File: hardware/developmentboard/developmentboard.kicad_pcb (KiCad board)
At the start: 2 copper layers, 207.5 x 78.1 mm, 35 parts, among them J1 SPI Header, J2 Power Header, J3 Key Channels, U1 ADS7960, U10 DRV5053, U11 DRV5053, U12 DRV5053, U13 DRV5053, U14 AP2138N-2.5, U2 DRV5053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

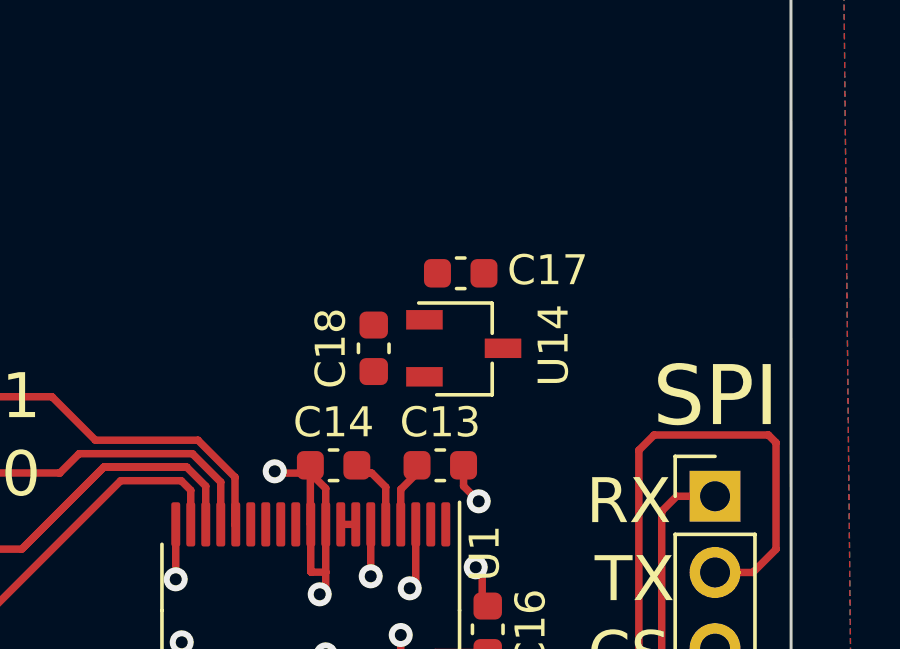
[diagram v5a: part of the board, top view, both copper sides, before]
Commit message: added reference IC to PCB, removed LDO
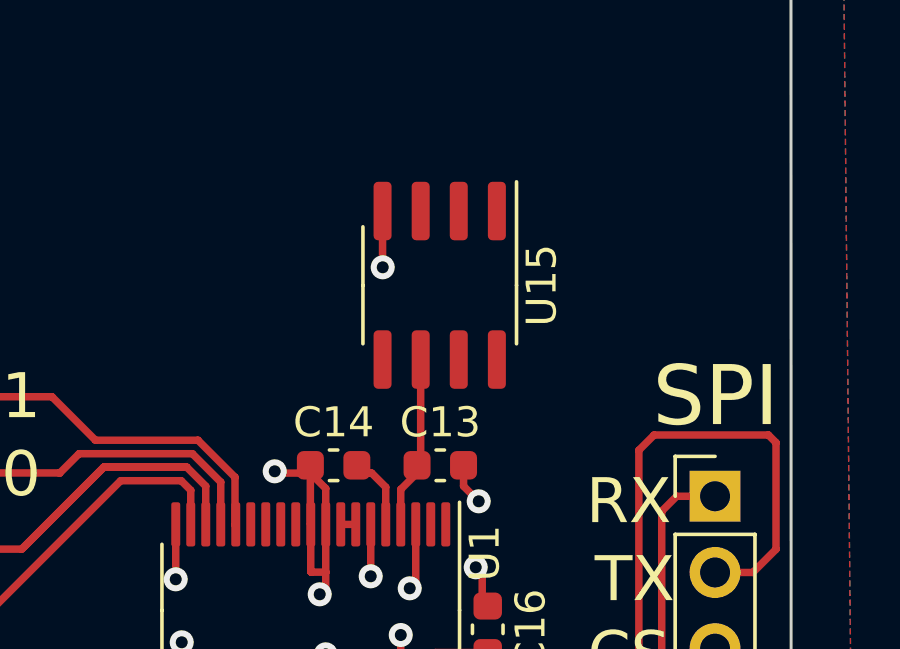
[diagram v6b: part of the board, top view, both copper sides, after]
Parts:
- removed C17, C18: 1uF, Capacitor_SMD:C_0603_1608Metric
- removed U14: AP2138N-2.5, Package_TO_SOT_SMD:TSOT-23
- added U15: REF5025AD, Package_SO:SOIC-8_3.9x4.9mm_P1.27mm, F.Cu at (249.4, 83.7)
- J3: value Key Channels -> Hall Effect Header
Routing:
- net +2V5: track 1.93 -> 5.51 mm
- net GND: track 54.4 -> 56.3 mm, vias 35 -> 36

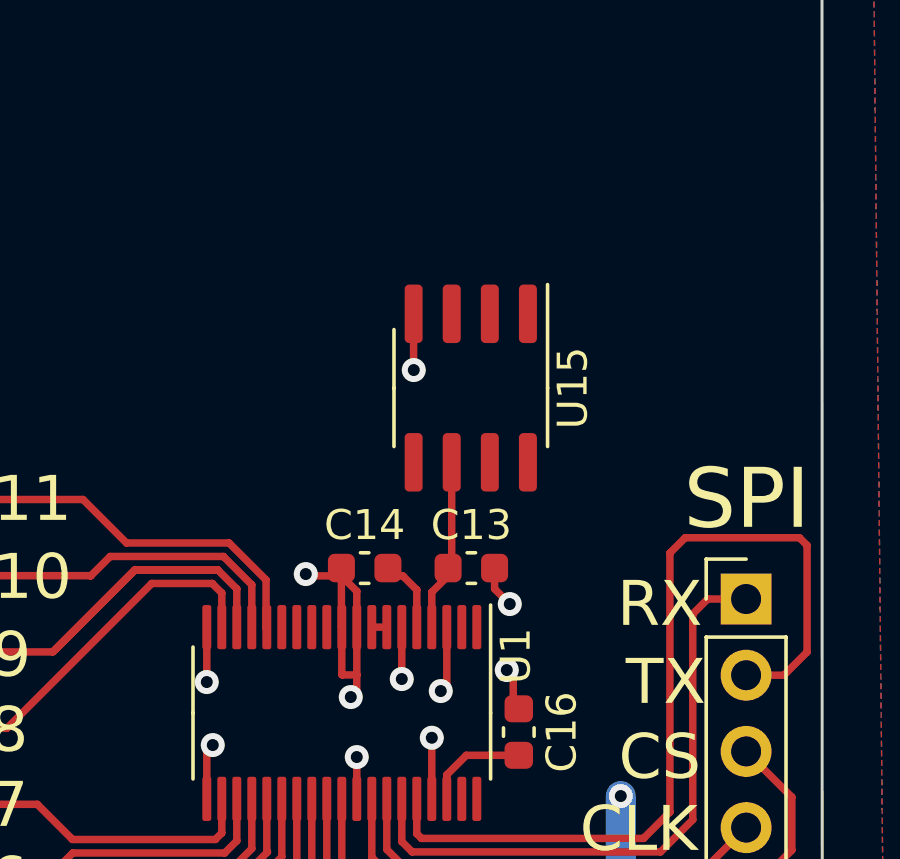
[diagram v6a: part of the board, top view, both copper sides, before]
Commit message: finalized reference IC pcb stuffs - added footprints for bypass caps
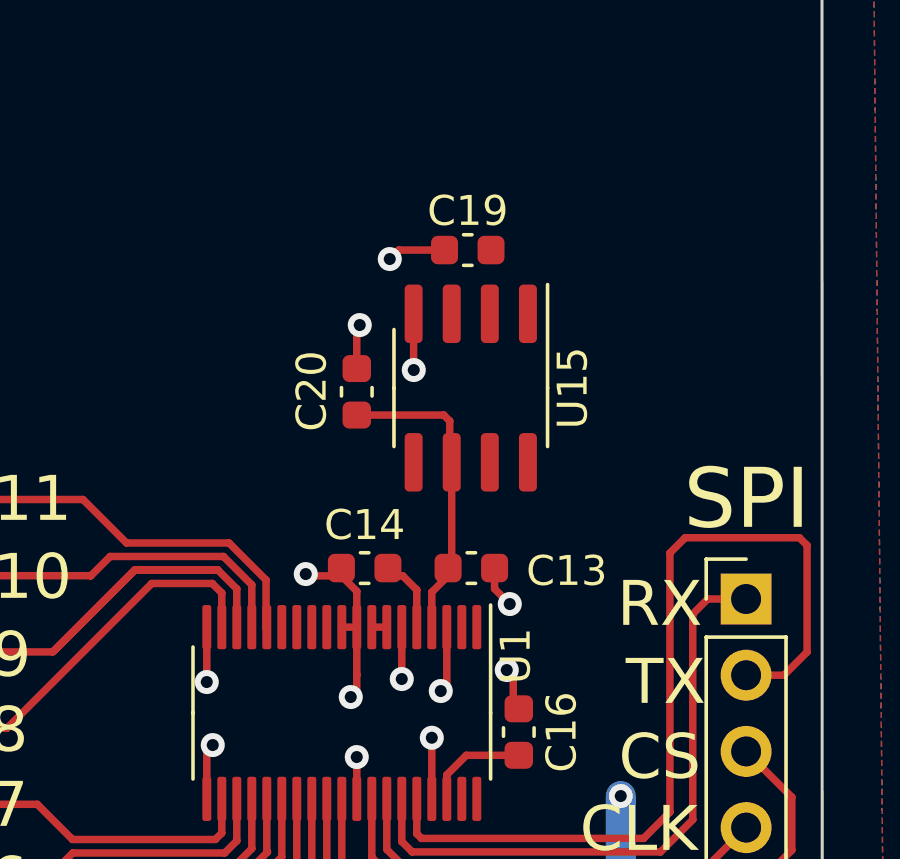
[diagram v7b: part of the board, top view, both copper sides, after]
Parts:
- added C19: 1-10uF, Capacitor_SMD:C_0603_1608Metric, F.Cu at (249.3, 79.1)
- added C20: 1-50uF, Capacitor_SMD:C_0603_1608Metric, F.Cu at (245.6, 83.8)
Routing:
- net +2V5: track 5.51 -> 10.1 mm
- net GND: track 56.3 -> 56.5 mm, vias 36 -> 38

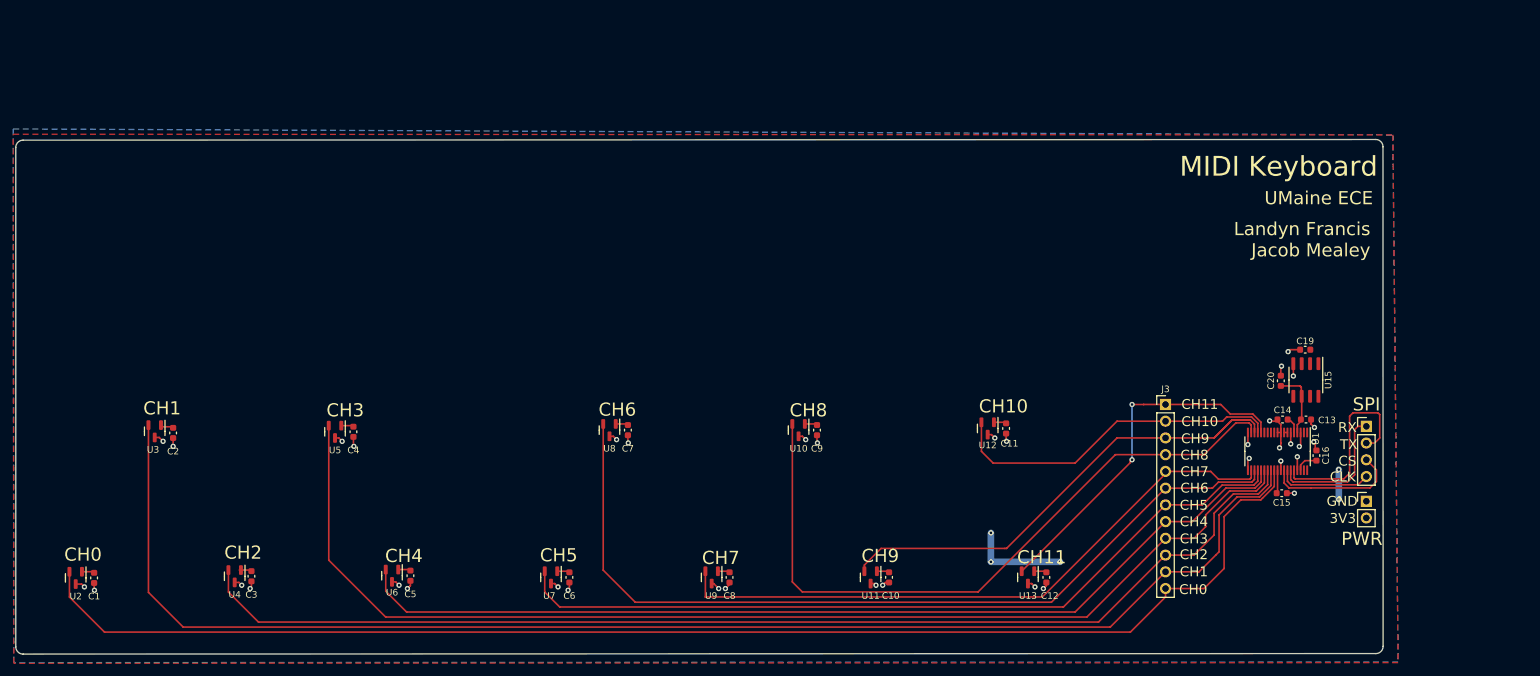
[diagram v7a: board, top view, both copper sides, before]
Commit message: mounting holes for keys board
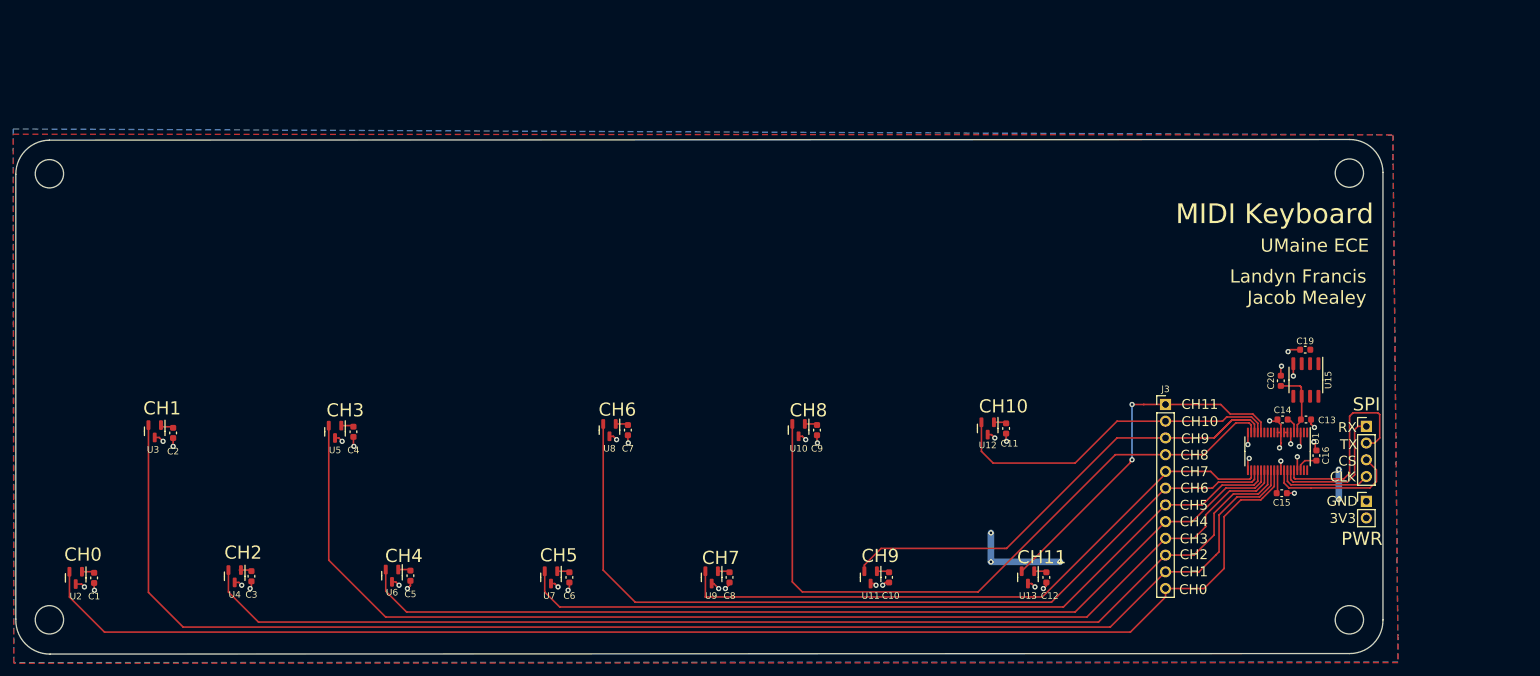
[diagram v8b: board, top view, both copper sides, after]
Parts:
- added REF**: MountingHole_4.3mm_M4, MountingHole:MountingHole_4.3mm_M4, F.Cu at (58.7, 120.1)
- added REF**: MountingHole_4.3mm_M4, MountingHole:MountingHole_4.3mm_M4, F.Cu at (256.0, 120.1)
- added REF**: MountingHole_4.3mm_M4, MountingHole:MountingHole_4.3mm_M4, F.Cu at (256.0, 52.3)
- added REF**: MountingHole_4.3mm_M4, MountingHole:MountingHole_4.3mm_M4, F.Cu at (58.7, 52.4)
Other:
- outline, holes or cut-outs redrawn
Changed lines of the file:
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@@
     )
+  )
+  (footprint "MountingHole:MountingHole_4.3mm_M4" (layer "F.Cu")
+    (at 58.694 120.056)
+    (descr "Mounting Hole 4.3mm, no annular, M4")
+    (tags "mounting hole 4.3mm no annular m4")
+    (attr exclude_from_pos_files exclude_from_bom)
+    (fp_text reference "REF**" (at 0 -5.3) (layer "F.SilkS") hide
+      (effects (font (size 1 1) (thickness 0.15)))
+    )
+    (fp_text value "MountingHole_4.3mm_M4" (at 0 5.3) (layer "F.Fab") hide
+      (effects (font (size 1 1) (thickness 0.15)))
+    )
+    (fp_text user "${REFERENCE}" (at 0 0) (layer "F.Fab")
+      (effects (font (size 1 1) (thickness 0.15)))
+    )
+    (fp_circle (center 0 0) (end 4.3 0) (layer "Cmts.User") (width 0.15) (fill none))
+    (fp_circle (center 0 0) (end 4.55 0) (layer "F.CrtYd") (width 0.05) (fill none))
+    (pad "" np_thru_hole circle (at 0 0) (size 4.3 4.3) (drill 4.3) (layers *.Cu *.Mask))
   )
   (footprint "Connector_PinHeader_2.54mm:PinHeader_1x02_P2.54mm_Vertical" (layer "F.Cu")
@@
       (rotate (xyz 0 0 0))
     )
+  )
+  (footprint "MountingHole:MountingHole_4.3mm_M4" (layer "F.Cu")
+    (at 255.994 120.056)
+    (descr "Mounting Hole 4.3mm, no annular, M4")
+    (tags "mounting hole 4.3mm no annular m4")
+    (attr exclude_from_pos_files exclude_from_bom)
+    (fp_text reference "REF**" (at 0 -5.3) (layer "F.SilkS") hide
+      (effects (font (size 1 1) (thickness 0.15)))
+    )
+    (fp_text value "MountingHole_4.3mm_M4" (at 0 5.3) (layer "F.Fab") hide
+      (effects (font (size 1 1) (thickness 0.15)))
+    )
+    (fp_text user "${REFERENCE}" (at 0 0) (layer "F.Fab")
+      (effects (font (size 1 1) (thickness 0.15)))
+    )
+    (fp_circle (center 0 0) (end 4.3 0) (layer "Cmts.User") (width 0.15) (fill none))
+    (fp_circle (center 0 0) (end 4.55 0) (layer "F.CrtYd") (width 0.05) (fill none))
+    (pad "" np_thru_hole circle (at 0 0) (size 4.3 4.3) (drill 4.3) (layers *.Cu *.Mask))
   )
   (footprint "Capacitor_SMD:C_0603_1608Metric" locked (layer "F.Cu")
@@
     )
   )
+  (footprint "MountingHole:MountingHole_4.3mm_M4" (layer "F.Cu")
+    (at 255.994 52.256)
+    (descr "Mounting Hole 4.3mm, no annular, M4")
+    (tags "mounting hole 4.3mm no annular m4")
+    (attr exclude_from_pos_files exclude_from_bom)
+    (fp_text reference "REF**" (at 0 -5.3) (layer "F.SilkS") hide
+      (effects (font (size 1 1) (thickness 0.15)))
+    )
+    (fp_text value "MountingHole_4.3mm_M4" (at 0 5.3) (layer "F.Fab") hide
+      (effects (font (size 1 1) (thickness 0.15)))
+    )
+    (fp_text user "${REFERENCE}" (at 0 0) (layer "F.Fab")
+      (effects (font (size 1 1) (thickness 0.15)))
+    )
+    (fp_circle (center 0 0) (end 4.3 0) (layer "Cmts.User") (width 0.15) (fill none))
+    (fp_circle (center 0 0) (end 4.55 0) (layer "F.CrtYd") (width 0.05) (fill none))
+    (pad "" np_thru_hole circle (at 0 0) (size 4.3 4.3) (drill 4.3) (layers *.Cu *.Mask))
+  )
   (footprint "Package_TO_SOT_SMD:SOT-23" locked (layer "F.Cu")
     (at 143.698 91.2645 -90)
@@
       (rotate (xyz 0 0 0))
     )
+  )
+  (footprint "MountingHole:MountingHole_4.3mm_M4" (layer "F.Cu")
+    (at 58.694 52.356)
+    (descr "Mounting Hole 4.3mm, no annular, M4")
+    (tags "mounting hole 4.3mm no annular m4")
+    (attr exclude_from_pos_files exclude_from_bom)
+    (fp_text reference "REF**" (at 0 -5.3) (layer "F.SilkS") hide
+      (effects (font (size 1 1) (thickness 0.15)))
+    )
+    (fp_text value "MountingHole_4.3mm_M4" (at 0 5.3) (layer "F.Fab") hide
+      (effects (font (size 1 1) (thickness 0.15)))
+    )
+    (fp_text user "${REFERENCE}" (at 0 0) (layer "F.Fab")
+      (effects (font (size 1 1) (thickness 0.15)))
+    )
+    (fp_circle (center 0 0) (end 4.3 0) (layer "Cmts.User") (width 0.15) (fill none))
+    (fp_circle (center 0 0) (end 4.55 0) (layer "F.CrtYd") (width 0.05) (fill none))
+    (pad "" np_thru_hole circle (at 0 0) (size 4.3 4.3) (drill 4.3) (layers *.Cu *.Mask))
   )
   (footprint "Capacitor_SMD:C_0603_1608Metric" locked (layer "F.Cu")
@@
     )
   )
-  (gr_arc (start 261.116183 124.078183) (mid 260.794 124.856) (end 260.016183 125.178183) (layer "Edge.Cuts") (width 0.1))
-  (gr_arc (start 259.994 47.156) (mid 260.771817 47.478183) (end 261.094 48.256) (layer "Edge.Cuts") (width 0.1))
-  (gr_line (start 261.094 48.256) (end 261.116183 124.078183) (layer "Edge.Cuts") (width 0.1))
-  (gr_line (start 260.016183 125.178183) (end 54.694 125.256) (layer "Edge.Cuts") (width 0.1))
-  (gr_arc (start 53.594 48.356) (mid 53.916183 47.578183) (end 54.694 47.256) (layer "Edge.Cuts") (width 0.1))
-  (gr_line (start 53.594 124.156) (end 53.594 48.356) (layer "Edge.Cuts") (width 0.1))
-  (gr_line (start 54.694 47.256) (end 259.994 47.156) (layer "Edge.Cuts") (width 0.1))
-  (gr_arc (start 54.694 125.256) (mid 53.916183 124.933817) (end 53.594 124.156) (layer "Edge.Cuts") (width 0.1))
-  (gr_text "Designed in Orono ME " (at 74.294 121.556) (layer "B.SilkS")
+  (gr_arc (start 261.094 120.056) (mid 259.624804 123.693215) (end 255.994 125.178183) (layer "Edge.Cuts") (width 0.1))
+  (gr_arc (start 255.994 47.156) (mid 259.586219 48.592936) (end 261.094 52.156) (layer "Edge.Cuts") (width 0.1))
+  (gr_line (start 261.094 52.156) (end 261.094 120.056) (layer "Edge.Cuts") (width 0.1))
+  (gr_line (start 255.994 125.178183) (end 58.794 125.256) (layer "Edge.Cuts") (width 0.1))
+  (gr_arc (start 53.594 52.456) (mid 55.069856 48.802511) (end 58.694 47.256) (layer "Edge.Cuts") (width 0.1))
+  (gr_line (start 53.594 119.956) (end 53.594 52.456) (layer "Edge.Cuts") (width 0.1))
+  (gr_line (start 58.694 47.256) (end 255.994 47.156) (layer "Edge.Cuts") (width 0.1))
+  (gr_arc (start 58.794 125.256) (mid 55.062701 123.715952) (end 53.594 119.956) (layer "Edge.Cuts") (width 0.1))
+  (gr_text "Designed in Orono ME " (at 83.194 121.156) (layer "B.SilkS")
     (effects (font (size 2 2) (thickness 0.3)) (justify mirror))
   )
@@
     (effects (font (size 1.5 1.5) (thickness 0.3)))
   )
-  (gr_text "MIDI Keyboard" (at 260.294 51.256) (layer "F.SilkS")
+  (gr_text "MIDI Keyboard" (at 259.694 58.456) (layer "F.SilkS")
     (effects (font (size 3 3) (thickness 0.3)) (justify right))
   )
-  (gr_text "UMaine ECE" (at 259.594 56.056) (layer "F.SilkS")
+  (gr_text "UMaine ECE" (at 258.994 63.256) (layer "F.SilkS")
     (effects (font (size 2 2) (thickness 0.3)) (justify right))
   )
@@
     (effects (font (size 2 2) (thickness 0.3)))
   )
-  (gr_text "Landyn Francis\nJacob Mealey" (at 259.194 62.356) (layer "F.SilkS")
+  (gr_text "Landyn Francis\nJacob Mealey" (at 258.594 69.556) (layer "F.SilkS")
     (effects (font (size 2 2) (thickness 0.3)) (justify right))
   )
